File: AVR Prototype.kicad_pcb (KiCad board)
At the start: 4 copper layers, 131.1 x 42.9 mm, 37 parts, among them J1 Barrel_Jack_Switch, J2 AVR-ISP, J3 Aux, J4 Conn_01x06, J5 ConnA, J6 ConnB, J7 Conn_01x03, T1 R-78E5.0-1.0, T2 R-78E3.3-1.0, U1 ATxmega256A3U-AU, Y1 16 MHz

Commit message: Routed by FreeRouting
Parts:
- removed the FB1 at (77.2, 85.0)
- removed FB2, FB3, FB4, FB5: Fe, Resistor_SMD:R_0805_2012Metric_Pad1.20x1.40mm_HandSolder
- added C16: 10 uF, Capacitor_THT:C_Radial_D6.3mm_H11.0mm_P2.50mm, F.Cu at (66.5, 81.0)
- added C9: 10 uF, Capacitor_THT:C_Radial_D6.3mm_H11.0mm_P2.50mm, F.Cu at (74.4, 81.0)
- added L3: 10 uH, BRG_Footprints:SBT0210, F.Cu at (65.3, 88.6)
- C1: renamed from C7; value 22 pF -> 10 pF
- C10: renamed from C1; footprint Capacitor_THT:C_Rect_L13.5mm_W5.0mm_P10.00mm_FKS3_FKP3_MKS4 -> Capacitor_SMD:C_2220_5650Metric_Pad1.97x5.40mm_HandSolder
- C11: renamed from C2; footprint Capacitor_THT:C_Rect_L13.5mm_W5.0mm_P10.00mm_FKS3_FKP3_MKS4 -> Capacitor_SMD:C_2220_5650Metric_Pad1.97x5.40mm_HandSolder
- C14: renamed from C5; value 0.1 uF -> 0.1uF
- C15: renamed from C6; value 0.1 uF -> 0.1uF
- C2: renamed from C8; value 22 pF -> 10 pF
- moved C12 28.3 mm to (45.0, 94.5)
- moved C13 21.1 mm to (49.8, 94.5)
- moved C14 18.2 mm to (54.6, 94.5)
- moved L1 16.1 mm to (47.2, 80.3)
- moved L2 15.8 mm to (47.2, 88.4)
- moved C10 11.2 mm to (56.9, 80.3)
- moved C15 11.1 mm to (59.2, 94.5)
- moved C11 5.64 mm to (56.9, 88.4)
- moved FB1 5.13 mm to (85.3, 74.9)
- moved C6 2.80 mm to (104.1, 74.9)
- moved C5 2.54 mm to (104.1, 98.0)
- moved C4 1.65 mm to (82.5, 98.0)
- moved C7 1.34 mm to (90.4, 74.9)
- moved C8 1.34 mm to (80.2, 74.9)
- renumbered C3 to C12, C4 to C13, C9 to C3, C10 to C4, C11 to C5, C12 to C6, C13 to C7, C14 to C8, FB6 to FB1, J2 to J1, J3 to J2, J4 to J3, J5 to J4, J6 to J5, J1 to J6, R2 to R1, R1 to R2
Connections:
- C8 pad 2: +3V3 -> Net-(C8-Pad2)
- FB1 pad 1: Net-(FB6-Pad1) -> +3V3
- FB1 pad 2: +3V3 -> Net-(C8-Pad2)
- J1 pad 3: (no net) -> unconnected-(J1-Pad3)
- J1 pad 4: (no net) -> unconnected-(J1-Pad4)
- J3 pad 2: (no net) -> unconnected-(J3-Pad2)
- J3 pad 3: (no net) -> unconnected-(J3-Pad3)
- J3 pad 4: (no net) -> unconnected-(J3-Pad4)
- J3 pad 6: (no net) -> unconnected-(J3-Pad6)
- J6 pad 3: (no net) -> unconnected-(J6-Pad3)
- S1 pad 3: (no net) -> unconnected-(S1-Pad3)
- U1 pad 15: Net-(FB1-Pad2) -> +3V3
- U1 pad 25: Net-(FB2-Pad1) -> +3V3
- U1 pad 35: Net-(FB3-Pad2) -> +3V3
- U1 pad 45: Net-(FB4-Pad1) -> +3V3
- U1 pad 53: Net-(FB5-Pad2) -> +3V3
- U1 pad 61: Net-(FB6-Pad1) -> Net-(C8-Pad2)
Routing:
- net /PIN_01: track 95.9 -> 68.9 mm, vias 0 -> 1
- net Net-(C8-Pad2): track 0.00 -> 21.5 mm
- net /Power/5Vb: track 36.4 -> 19.9 mm
- net Net-(FB2-Pad1): track 15.9 -> 0.00 mm, vias 2 -> 0
- net +5V: track 164.2 -> 149.1 mm, vias 0 -> 1
- net Net-(FB6-Pad1): track 12.3 -> 0.00 mm
- net Net-(FB1-Pad2): track 10.9 -> 0.00 mm
- net /PIN_30: track 14.9 -> 24.8 mm
- net /PIN_11: track 45.4 -> 35.6 mm
- net Net-(FB4-Pad1): track 9.03 -> 0.00 mm, vias 2 -> 0
- net /PIN_13: track 37.8 -> 29.9 mm
- net Net-(FB3-Pad2): track 7.94 -> 0.00 mm
- net Net-(FB5-Pad2): track 7.86 -> 0.00 mm, vias 2 -> 0
- net /Power/9Vb: track 36.0 -> 42.1 mm
- net /PIN_09: track 47.1 -> 41.5 mm
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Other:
- board text added: "AVR ATXMEGA 256 A3U Prototype Board (V2) (c) 2023 Brian Good License: CC BY 4.0 creativecommons.org/licenses/BY/4.0/"
- board text removed: "AVR ATXMEGA 256 A3U Prototype Board (c) 2022 Brian Good License: CC BY 4.0 creativecommons.org/licenses/BY/4.0/"

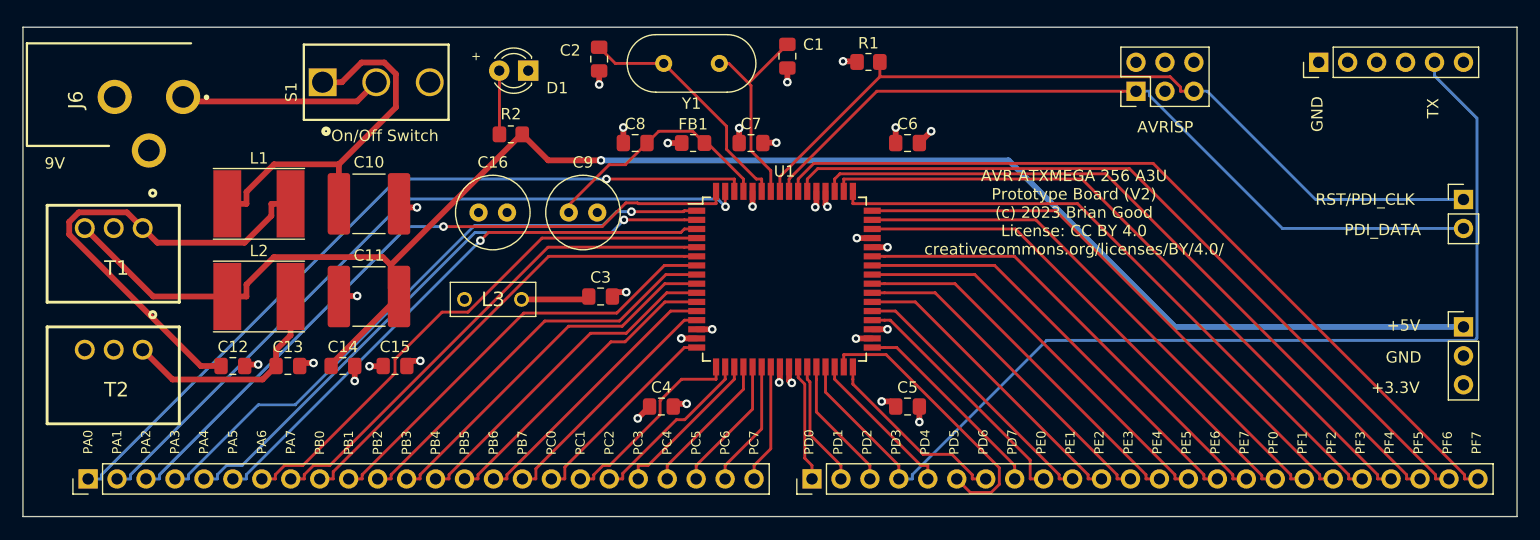
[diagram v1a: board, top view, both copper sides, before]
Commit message: Updated V3.3 Converter to VCC input
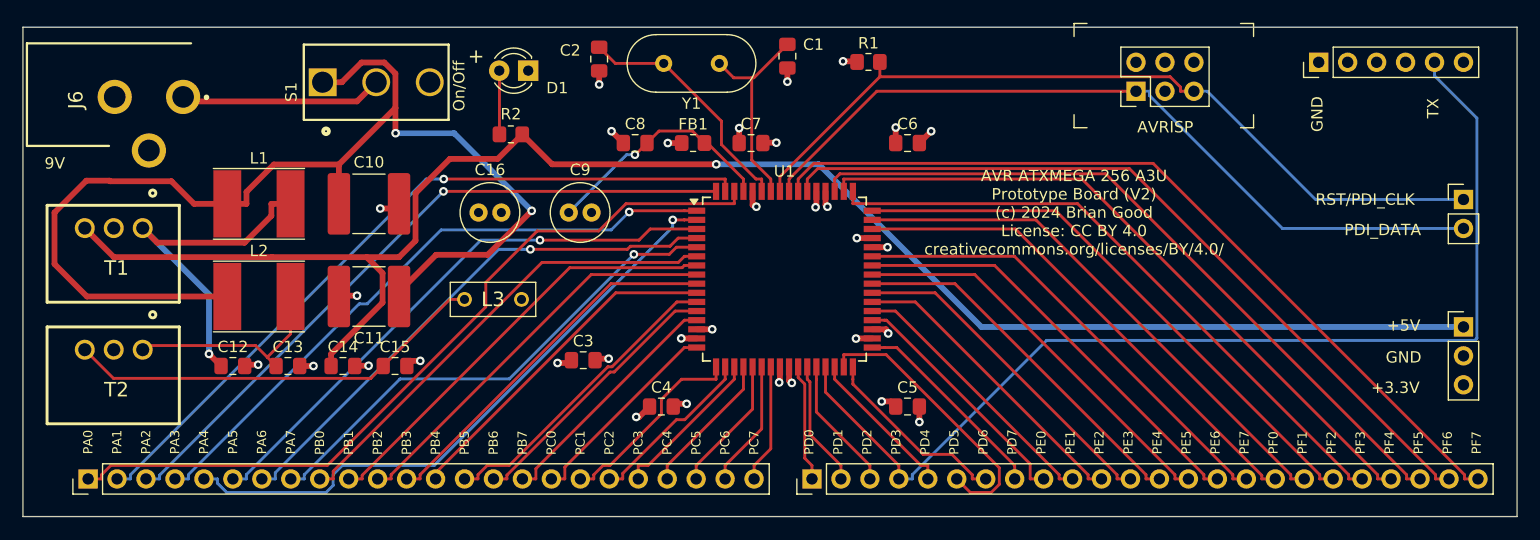
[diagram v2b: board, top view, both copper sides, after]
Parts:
- C10, C11: footprint Capacitor_SMD:C_2220_5650Metric_Pad1.97x5.40mm_HandSolder -> Capacitor_SMD:C_2220_5750Metric_Pad1.97x5.40mm_HandSolder
- C16, C9: footprint Capacitor_THT:C_Radial_D6.3mm_H11.0mm_P2.50mm -> Capacitor_THT:C_Radial_D5.0mm_H11.0mm_P2.00mm
- S1: value On/Off Switch -> On/Off
- moved C3 5.79 mm to (75.7, 94.0)
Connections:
- net /Power/5Vb renamed Net-(T2-+VIN)
- C11 pad 1: +5V -> VCC
- C15 pad 1: +3V3 -> Net-(T2-+VOUT)
- L2 pad 1: +5V -> VCC
- L3 pad 1: +3V3 -> Net-(T2-+VOUT)
- T2 pad 3: +3V3 -> Net-(T2-+VOUT)
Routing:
- net VCC: track 32.9 -> 102.8 mm, vias 0 -> 2
- net Net-(T2-+VOUT): track 0.00 -> 37.2 mm
- net /Power/9Vb: track 42.1 -> 30.5 mm, vias 0 -> 1
- net +3V3: track 22.2 -> 16.6 mm
- net /PIN_05: track 52.9 -> 54.8 mm
- net +5V: track 149.1 -> 147.9 mm
- net Net-(T2-+VIN): track 19.9 -> 18.8 mm
- net /PIN_03: track 61.4 -> 60.6 mm
- net /PIN_07: track 47.8 -> 47.2 mm, vias 0 -> 1
- net /PIN_01: track 68.9 -> 69.2 mm, vias 1 -> 0
- net Net-(U1-AVCC): track 21.5 -> 21.1 mm, vias 0 -> 1
- net /PIN_08: vias 0 -> 1
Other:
- board text added: "AVR ATXMEGA 256 A3U Prototype Board (V2) (c) 2024 Brian Good License: CC BY 4.0 creativecommons.org/licenses/BY/4.0/"
- board text removed: "AVR ATXMEGA 256 A3U Prototype Board (V2) (c) 2023 Brian Good License: CC BY 4.0 creativecommons.org/licenses/BY/4.0/"
